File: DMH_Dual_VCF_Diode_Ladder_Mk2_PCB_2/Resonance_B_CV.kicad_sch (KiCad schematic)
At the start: 25 parts, among them J22 Conn_01x06_PinHeader, Q3 BC548, Q4 BC548, SW8 SW_DPDT_x2, U2 TL074

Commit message: Changed Resonance pots to Taper C type
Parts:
- RV22: value 100k -> C100k
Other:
- note added: "Inverted Log Pot"
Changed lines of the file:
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@@
+		)
+	)
+	(text "Inverted\nLog Pot"
+		(exclude_from_sim no)
+		(at 92.964 130.048 0)
+		(effects
+			(font
+				(size 1.27 1.27)
+				(italic yes)
+			)
 		)
 	)
@@
 			)
 		)
-		(property "Value" "100k"
+		(property "Value" "C100k"
 			(at 99.06 123.1901 0)
 			(effects

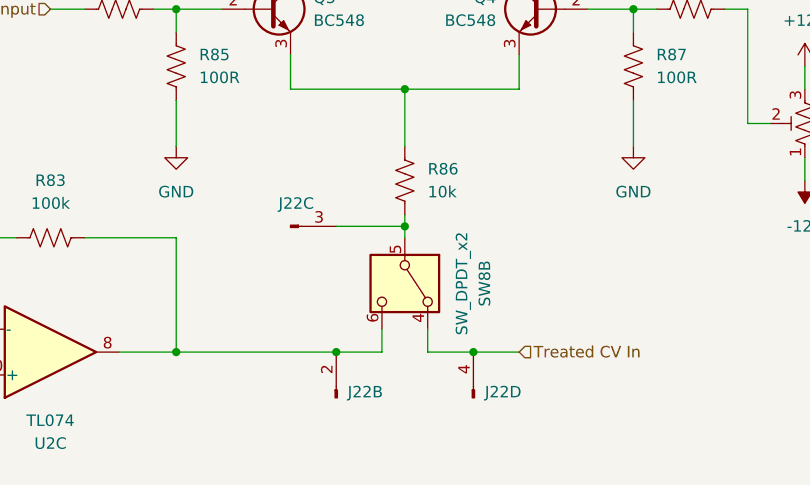
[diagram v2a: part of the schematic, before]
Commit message: Re-exported Gerbers
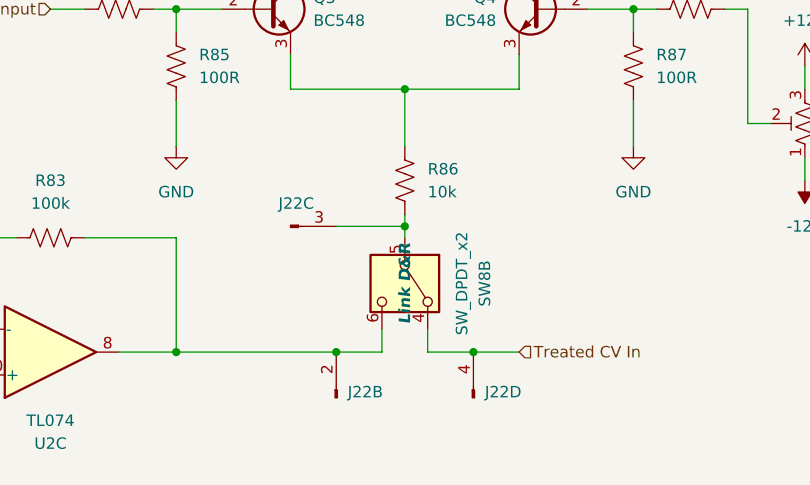
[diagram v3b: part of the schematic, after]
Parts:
- SW8: Function (none) -> Link D&R
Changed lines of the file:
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@@
+			)
+		)
+		(property "Function" "Link D&R"
+			(at 177.8 119.38 0)
+			(effects
+				(font
+					(size 1.27 1.27)
+					(thickness 0.254)
+					(bold yes)
+					(italic yes)
+				)
 			)
 		)
